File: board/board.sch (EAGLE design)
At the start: 66 parts, among them Q2 ULN2003AD

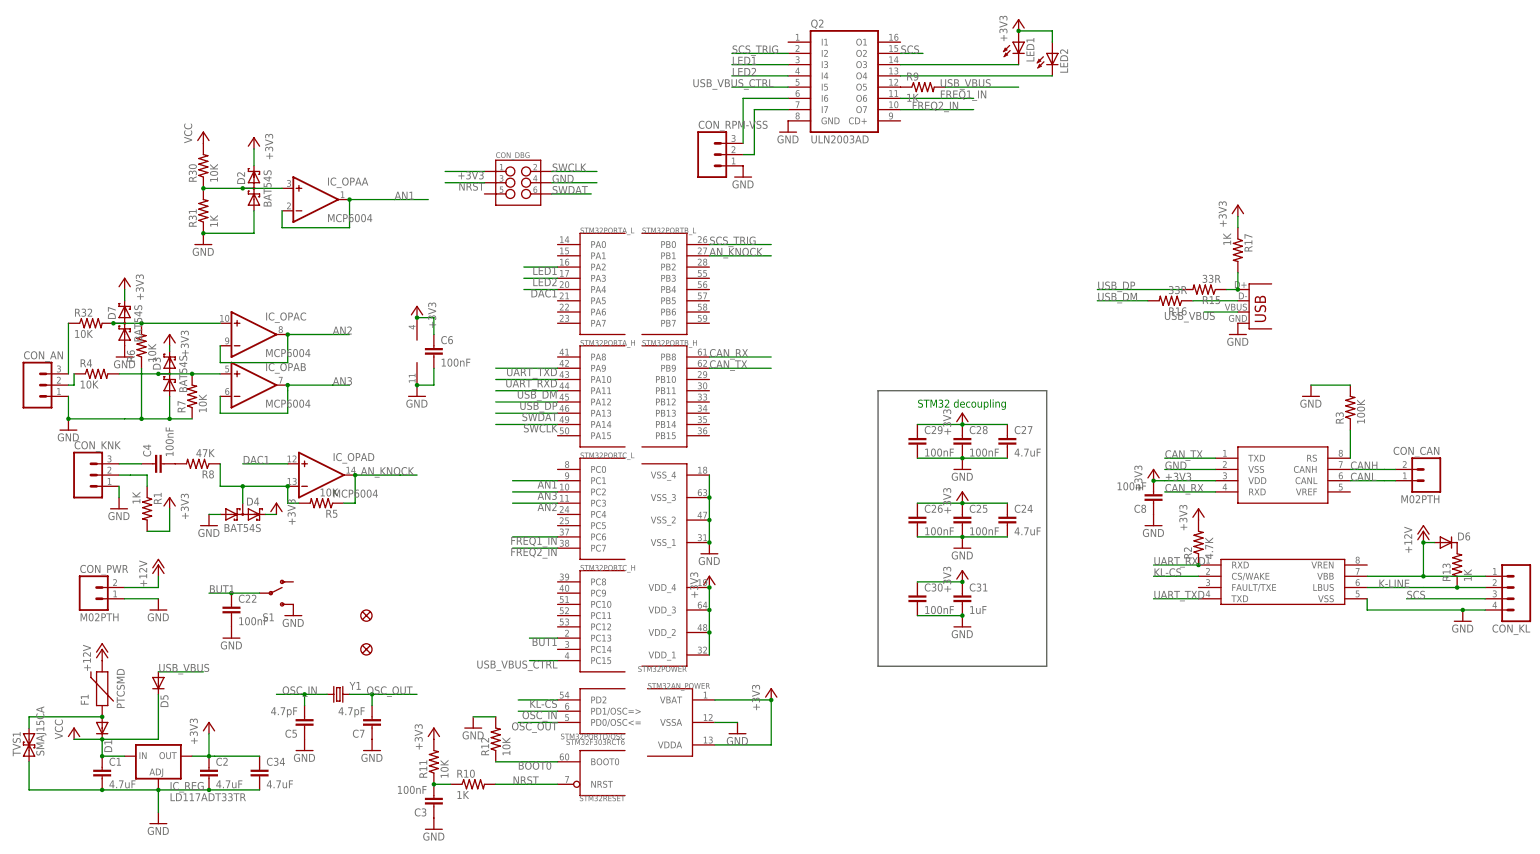
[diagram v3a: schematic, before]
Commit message: [Board] Adding output for external relay
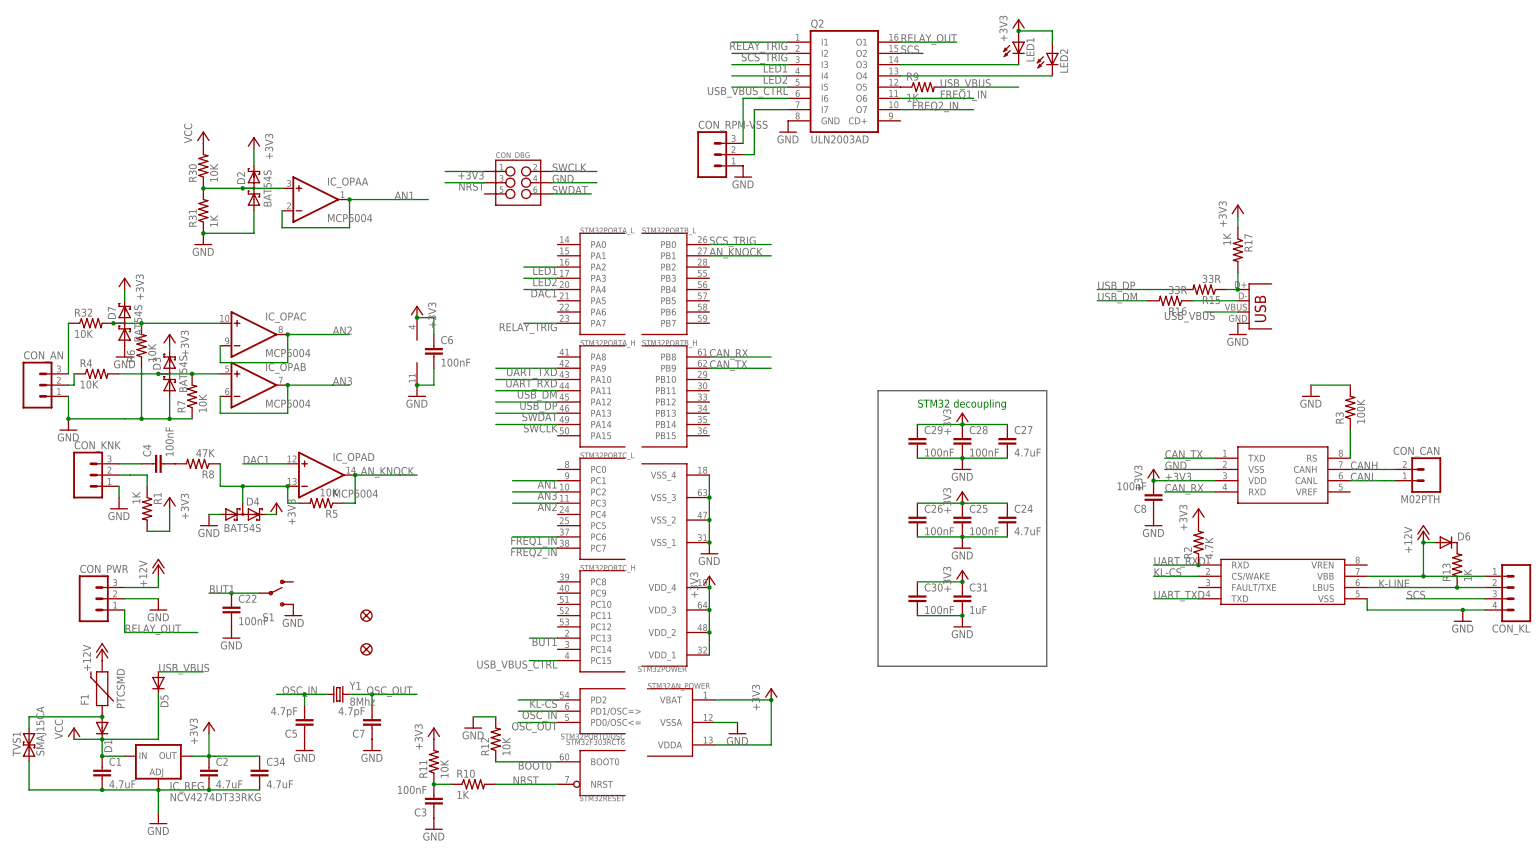
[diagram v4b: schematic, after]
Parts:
- CON_PWR: value M02PTH -> (none); device SparkFun-Connectors:M02PTH -> SparkFun-Connectors:M03PTH
- IC_REG: value LD117ADT33TR -> NCV4274DT33RKG
- Y1: value (none) -> 8Mhz
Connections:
- new net RELAY_OUT: CON_PWR.1, Q2.O1
- new net RELAY_TRIG: Q2.I1, STM32PORTA_L.PA7
- net +12V: now also CON_PWR.3; no longer CON_PWR.2
- net GND: now also CON_PWR.2; no longer CON_PWR.1
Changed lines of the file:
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@@
 </classes>
 <parts>
-<part name="IC_REG" library="v-reg" deviceset="LD117A?*" device="DT" technology="33TR"/>
+<part name="IC_REG" library="v-reg" deviceset="LD117A?*" device="DT" technology="33TR" value="NCV4274DT33RKG"/>
 <part name="GND1" library="supply1" deviceset="GND" device=""/>
 <part name="+3V1" library="supply1" deviceset="+3V3" device=""/>
@@
 <part name="GND6" library="supply1" deviceset="GND" device=""/>
 <part name="GND8" library="supply1" deviceset="GND" device=""/>
-<part name="CON_PWR" library="SparkFun-Connectors" deviceset="M02" device="PTH"/>
+<part name="CON_PWR" library="SparkFun-Connectors" deviceset="M03" device="PTH"/>
 <part name="GND9" library="supply1" deviceset="GND" device=""/>
 <part name="P+4" library="supply1" deviceset="+12V" device=""/>
@@
 <part name="R13" library="SparkFun-Resistors" deviceset="RESISTOR" device="0603-RES" value="1K"/>
 <part name="D6" library="SparkFun-DiscreteSemi" deviceset="DIODE" device="SMA"/>
-<part name="Y1" library="SparkFun-FreqCtrl" deviceset="CRYSTAL" device="HC49US"/>
+<part name="Y1" library="SparkFun-FreqCtrl" deviceset="CRYSTAL" device="HC49US" value="8Mhz"/>
 <part name="C5" library="SparkFun-Capacitors" deviceset="CAP" device="0603-CAP" value="4.7pF"/>
 <part name="C7" library="SparkFun-Capacitors" deviceset="CAP" device="0603-CAP" value="4.7pF"/>
@@
 </segment>
 <segment>
-<pinref part="CON_PWR" gate="G$1" pin="1"/>
-<wire x1="44.45" y1="58.42" x2="52.07" y2="58.42" width="0.1524" layer="91"/>
-<pinref part="GND9" gate="1" pin="GND"/>
-</segment>
-<segment>
 <pinref part="Q2" gate="A" pin="GND"/>
 <pinref part="GND13" gate="1" pin="GND"/>
@@
 <pinref part="GND14" gate="1" pin="GND"/>
 </segment>
+<segment>
+<pinref part="CON_PWR" gate="G$1" pin="2"/>
+<pinref part="GND9" gate="1" pin="GND"/>
+<wire x1="44.45" y1="58.42" x2="52.07" y2="58.42" width="0.1524" layer="91"/>
+</segment>
 </net>
 <net name="+3V3" class="0">
@@
 </segment>
 <segment>
-<pinref part="CON_PWR" gate="G$1" pin="2"/>
 <pinref part="P+4" gate="1" pin="+12V"/>
+<wire x1="52.07" y1="60.96" x2="52.07" y2="63.5" width="0.1524" layer="91"/>
+<pinref part="CON_PWR" gate="G$1" pin="3"/>
 <wire x1="44.45" y1="60.96" x2="52.07" y2="60.96" width="0.1524" layer="91"/>
-<wire x1="52.07" y1="60.96" x2="52.07" y2="63.5" width="0.1524" layer="91"/>
 </segment>
 <segment>
@@
 <segment>
 <wire x1="194.31" y1="173.99" x2="181.61" y2="173.99" width="0.1524" layer="91"/>
-<label x="172.72" y="173.99" size="1.778" layer="95"/>
+<label x="194.31" y="173.99" size="1.778" layer="95" rot="R180"/>
 <pinref part="Q2" gate="A" pin="I5"/>
 </segment>
@@
 <pinref part="Q2" gate="A" pin="I3"/>
 <wire x1="194.31" y1="179.07" x2="181.61" y2="179.07" width="0.1524" layer="91"/>
-<label x="181.61" y="179.07" size="1.778" layer="95"/>
+<label x="194.31" y="179.07" size="1.778" layer="95" rot="R180"/>
 </segment>
 <segment>
@@
 <pinref part="Q2" gate="A" pin="I4"/>
 <wire x1="194.31" y1="176.53" x2="181.61" y2="176.53" width="0.1524" layer="91"/>
-<label x="181.61" y="176.53" size="1.778" layer="95"/>
+<label x="194.31" y="176.53" size="1.778" layer="95" rot="R180"/>
 </segment>
 <segment>
@@
 <pinref part="Q2" gate="A" pin="I2"/>
 <wire x1="194.31" y1="181.61" x2="181.61" y2="181.61" width="0.1524" layer="91"/>
-<label x="181.61" y="181.61" size="1.778" layer="95"/>
+<label x="194.31" y="181.61" size="1.778" layer="95" rot="R180"/>
 </segment>
 <segment>
@@
 </segment>
 </net>
+<net name="RELAY_OUT" class="0">
+<segment>
+<pinref part="Q2" gate="A" pin="O1"/>
+<wire x1="219.71" y1="184.15" x2="232.41" y2="184.15" width="0.1524" layer="91"/>
+<label x="219.71" y="184.15" size="1.778" layer="95"/>
+</segment>
+<segment>
+<pinref part="CON_PWR" gate="G$1" pin="1"/>
+<wire x1="44.45" y1="55.88" x2="44.45" y2="50.8" width="0.1524" layer="91"/>
+<wire x1="44.45" y1="50.8" x2="60.96" y2="50.8" width="0.1524" layer="91"/>
+<label x="44.45" y="50.8" size="1.778" layer="95"/>
+</segment>
+</net>
+<net name="RELAY_TRIG" class="0">
+<segment>
+<pinref part="Q2" gate="A" pin="I1"/>
+<wire x1="194.31" y1="184.15" x2="181.61" y2="184.15" width="0.1524" layer="91"/>
+<label x="194.31" y="184.15" size="1.778" layer="95" rot="R180"/>
+</segment>
+<segment>
+<pinref part="STM32" gate="PORTA_L" pin="PA7"/>
+<wire x1="142.24" y1="120.65" x2="134.62" y2="120.65" width="0.1524" layer="91"/>
+<label x="142.24" y="120.65" size="1.778" layer="95" rot="R180"/>
+</segment>
+</net>

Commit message: [Board] Updated parts references
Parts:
- D1, D5, D6: value (none) -> B240A
- IC_REG: value NCV4274DT33RKG -> LM1117-3.3
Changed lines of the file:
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@@
 </classes>
 <parts>
-<part name="IC_REG" library="v-reg" deviceset="LD117A?*" device="DT" technology="33TR" value="NCV4274DT33RKG"/>
+<part name="IC_REG" library="v-reg" deviceset="LD117A?*" device="DT" technology="33TR" value="LM1117-3.3"/>
 <part name="GND1" library="supply1" deviceset="GND" device=""/>
 <part name="+3V1" library="supply1" deviceset="+3V3" device=""/>
@@
 <part name="C2" library="SparkFun-Passives" deviceset="CAP" device="0603-CAP" value="4.7uF"/>
 <part name="P+2" library="supply1" deviceset="+12V" device=""/>
-<part name="D1" library="SparkFun-DiscreteSemi" deviceset="DIODE" device="SMA"/>
+<part name="D1" library="SparkFun-DiscreteSemi" deviceset="DIODE" device="SMA" value="B240A"/>
 <part name="P+1" library="supply1" deviceset="VCC" device=""/>
 <part name="JP1" library="SparkFun-Connectors" deviceset="USB" device="SMD"/>
@@
 <part name="FID2" library="SparkFun-Aesthetics" deviceset="FIDUCIAL" device="1X2" value="FIDUCIAL1X2"/>
 <part name="R1" library="SparkFun-Resistors" deviceset="RESISTOR" device="0603-RES" value="1K"/>
-<part name="D5" library="SparkFun-DiscreteSemi" deviceset="DIODE" device="SMA"/>
+<part name="D5" library="SparkFun-DiscreteSemi" deviceset="DIODE" device="SMA" value="B240A"/>
 <part name="TVS1" library="SparkFun-DiscreteSemi" deviceset="TVS" device="" value="SMAJ15CA"/>
 <part name="R2" library="SparkFun-Resistors" deviceset="RESISTOR" device="0603-RES" value="4.7K"/>
@@
 <part name="IC_KLINE" library="misc" deviceset="MCP2004" device=""/>
 <part name="R13" library="SparkFun-Resistors" deviceset="RESISTOR" device="0603-RES" value="1K"/>
-<part name="D6" library="SparkFun-DiscreteSemi" deviceset="DIODE" device="SMA"/>
+<part name="D6" library="SparkFun-DiscreteSemi" deviceset="DIODE" device="SMA" value="B240A"/>
 <part name="Y1" library="SparkFun-FreqCtrl" deviceset="CRYSTAL" device="HC49US" value="8Mhz"/>
 <part name="C5" library="SparkFun-Capacitors" deviceset="CAP" device="0603-CAP" value="4.7pF"/>
